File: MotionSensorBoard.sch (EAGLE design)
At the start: 26 parts, among them J1 PRGM, J2 POWER_JACKPTH, U1 ATTINY2313A-SUR, U2 ISO7221ADR, U4 NCP1117ST50T3G, U5 LM1117MPX-3.3

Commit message: updated schematic
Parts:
- removed C5: 0.1uF, SparkFun-Passives:CAP0603-CAP
- removed C8: 10uF, Passives:CAP_POL_AL
- removed JP2: (no value), SparkFun-Connectors:M07
- removed S1: SWITCH, SparkFun-Electromechanical:SWITCH-MOMENTARY-2PTH
- removed Y2: (no value), SparkFun-FreqCtrl:RESONATORPTH
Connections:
- removed net N$1: U1.XTAL2, Y2.1
- removed net N$2: U1.XTAL1, Y2.3
- removed net N$3: JP2.7, U1.PB4
- removed net N$4: JP2.6, U1.PB3
- removed net N$5: JP2.5, U1.PB2
- removed net N$6: JP2.4, U1.PB1
- net 3.3V: no longer JP2.2
- net GND: now also JP1.1; no longer C5.2, C8.-, JP1.3, JP2.1, S1.1, Y2.2
- net RESET: no longer C5.1, S1.2
- net SIGIN: now also JP1.3; no longer JP1.1, JP2.3
- net VIN: no longer C8.+
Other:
- moved on the sheet: C3, C4, R1, U$2, U1, U2

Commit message: Schematic Updated
Schematic Rev A major revisions complete
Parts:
- removed U1: ATTINY2313A-SUR, microcontrollers-atmel:ATTINY2313A-SUR
- added JP4: M02PTH, SparkFun-Connectors:M02PTH
- added Q1, Q2: BSS138, SparkFun-DiscreteSemi:MOSFET-NCHANNELBSS123LT1G
- added R2, R3, R6, R7: 4.7k, SparkFun-Resistors:RESISTOR0603
- added R4: PHOTOCELLPTH, SparkFun-Sensors:PHOTOCELLPTH
- added R5: 10k, SparkFun-Resistors:RESISTOR0603
- added U3: BMP180, SparkFun-Sensors:BMP180
- added U6: HTU21DSMD, SparkFun-Sensors:HTU21DSMD
- added U7: ATMEGA328P, SparkFun-DigitalIC:ATMEGA328_SMT
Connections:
- new net LHT: R4.P$1, R5.2, U7.PC0(ADC0)
- new net SCL_3_3V: Q2.S, R2.1, U3.SCL, U6.SCK
- new net SCL_5V: Q2.D, R6.1, U7.PC5(ADC5/SCL)
- new net SDA_3_3V: Q1.S, R3.1, U3.SDA, U6.DATA
- new net SDA_5V: Q1.D, R7.1, U7.PC4(ADC4/SDA)
- net 3.3V: now also Q1.G, Q2.G, R2.2, R3.2, U3.VDD, U3.VDDIO, U6.VDD
- net 5V: now also R4.P$2, R6.2, R7.2, U7.AVCC, U7.VCC@1, U7.VCC@2; no longer U1.VCC
- net GND: now also JP4.1, R5.1, U3.GND, U6.GND@2, U6.GND@7, U7.AGND, U7.GND@1, U7.GND@2; no longer U1.GND
- net MISO: now also U7.PB4(MISO); no longer U1.PB6
- net MOSI: now also U7.PB3(MOSI/OC2); no longer U1.PB5
- net RESET: now also U7.PC6(/RESET); no longer U1.!RESET
- net RXD: now also U7.PD0(RXD); no longer U1.RXD
- net SCK: now also U7.PB5(SCK); no longer U1.PB7
- net SIGIN: now also U7.PD5(T1); no longer U1.PB0
- net TXD: now also U7.PD1(TXD); no longer U1.TXD
- net VIN: now also JP4.2
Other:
- note added: "A"
- note added: "Ambient Light Sensor"
- note added: "Pressure Sensor"
- note added: "Temperature and Humidity Sensor"
- note removed: "0"
- moved on the sheet: C1, C2, C7, J1, J2, JP1, LED4, R1, R10, U4, U5

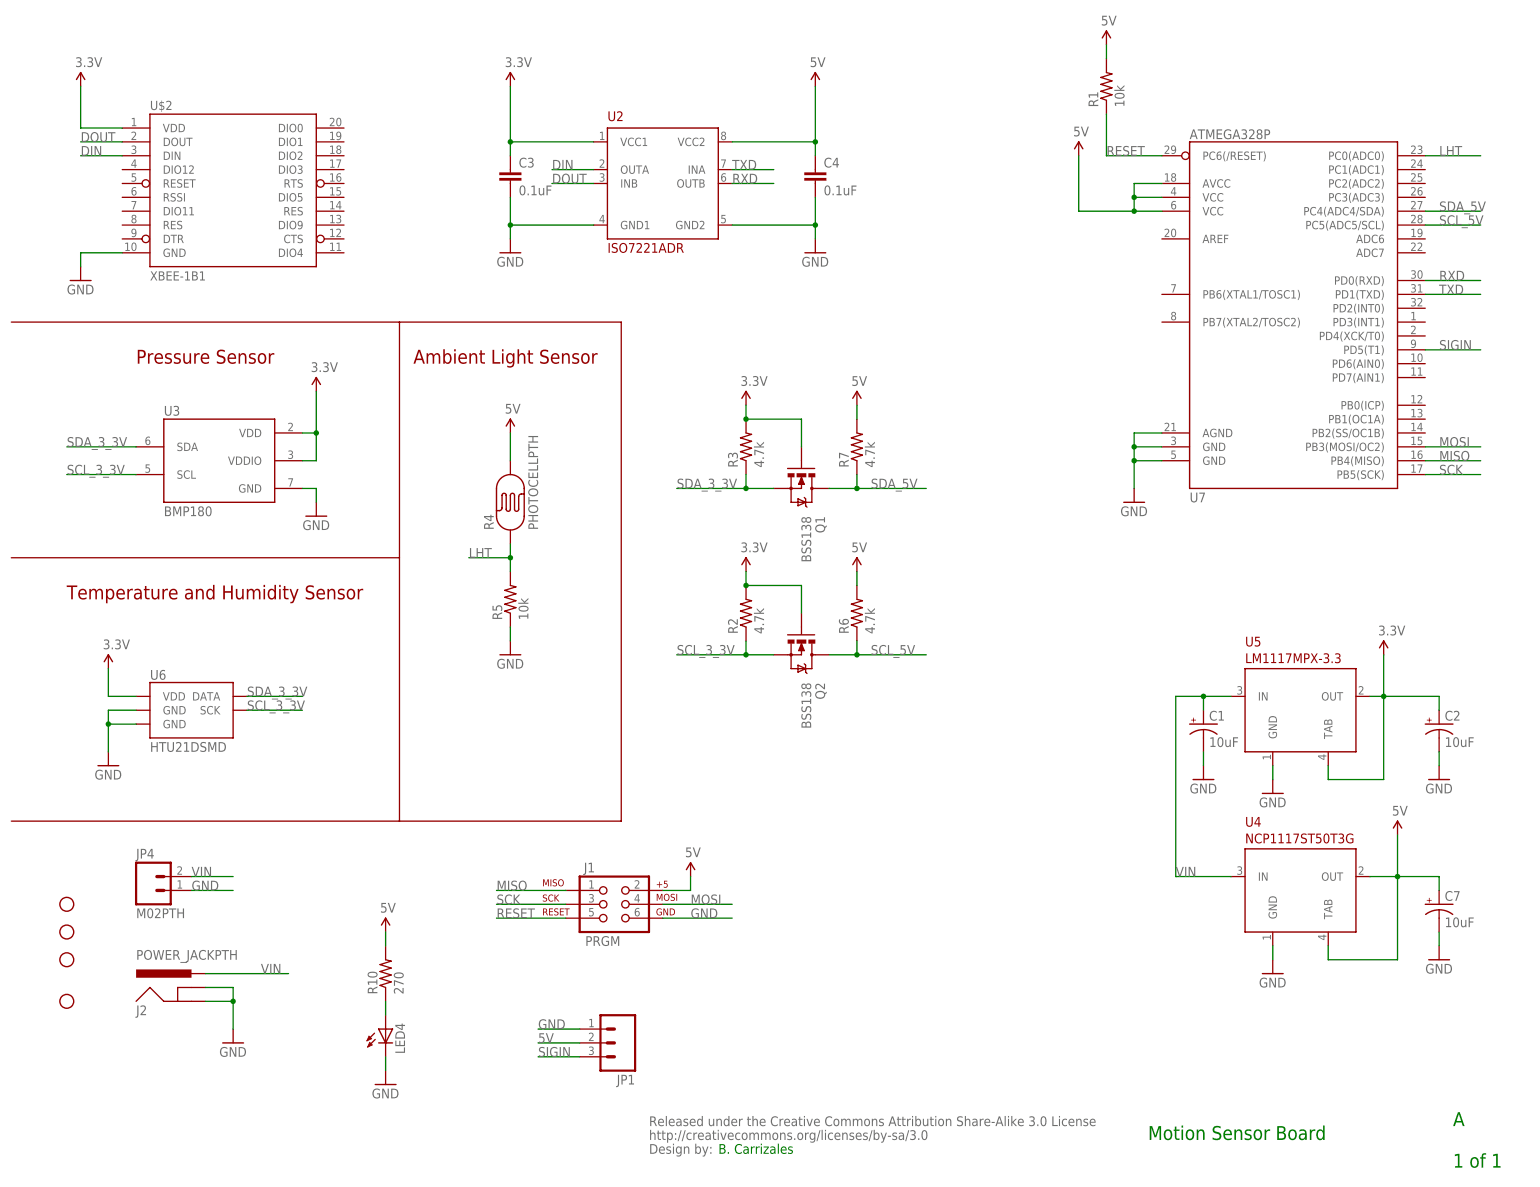
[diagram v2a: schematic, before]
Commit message: updated board layout and generated Gerbers
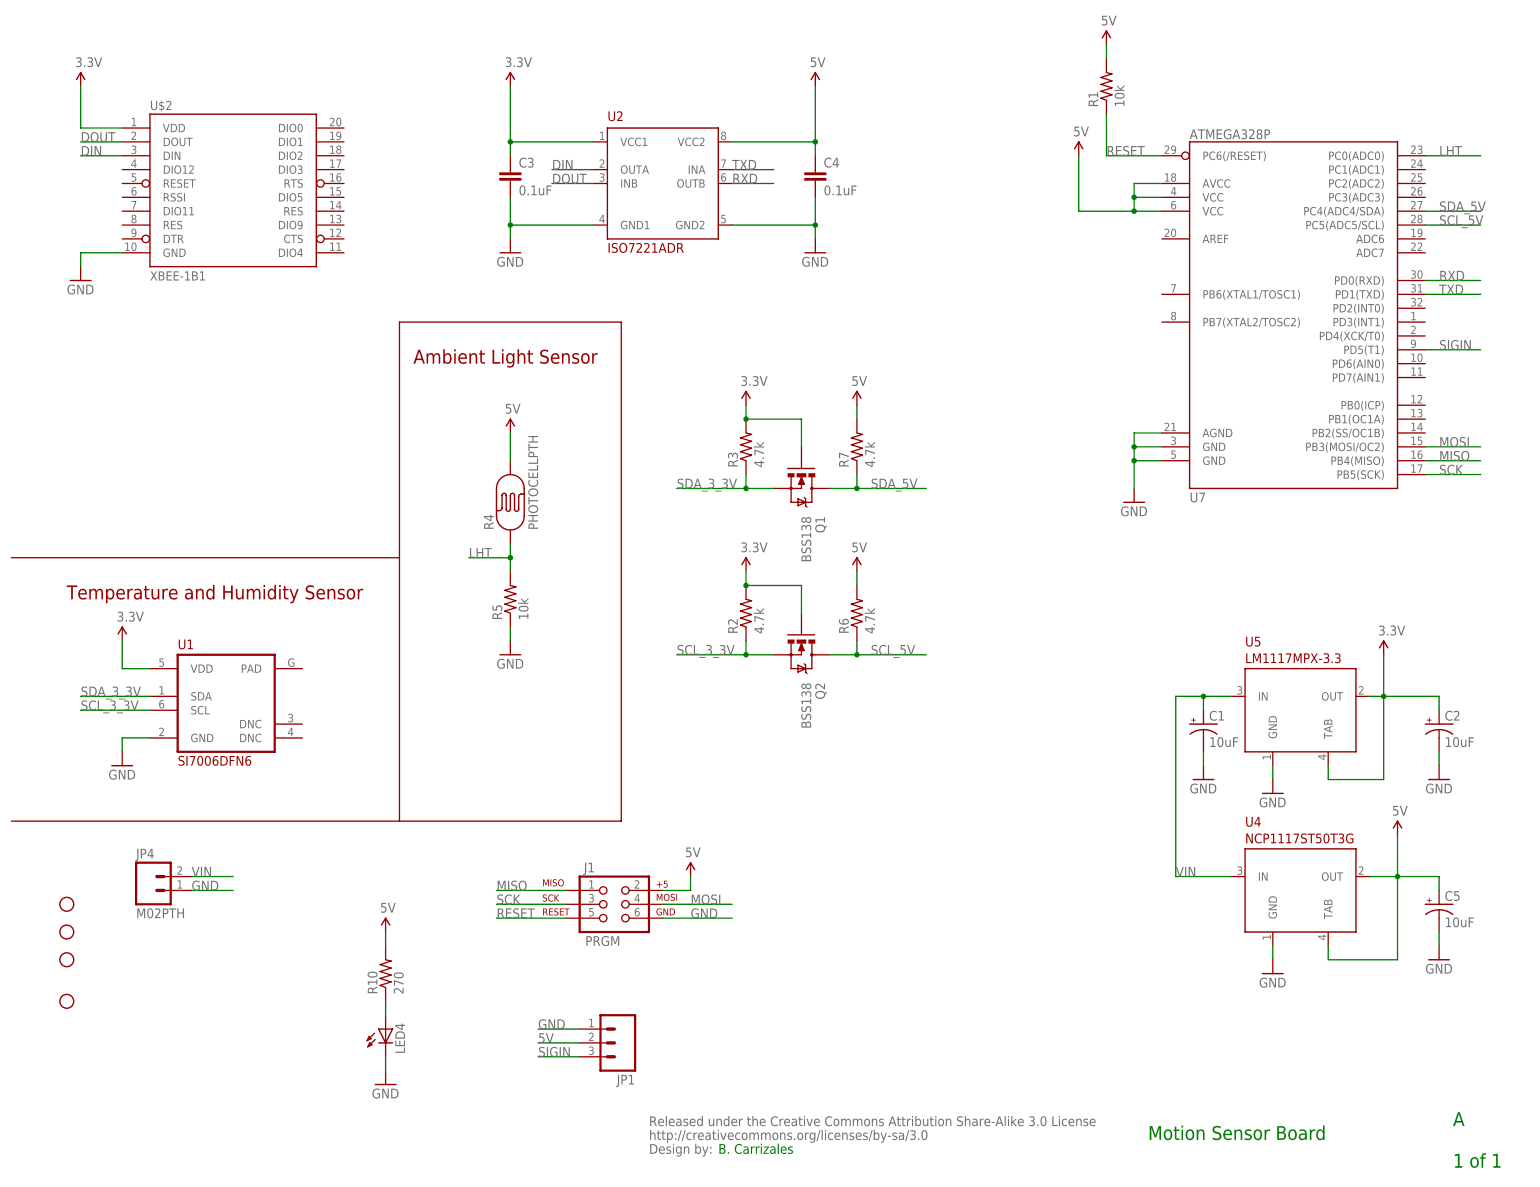
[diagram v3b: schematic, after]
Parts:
- removed C7: 10uF, Passives:CAP_POL_AL
- removed J2: POWER_JACKPTH, SparkFun-Connectors:POWER_JACKPTH
- removed U3: BMP180, SparkFun-Sensors:BMP180
- removed U6: HTU21DSMD, SparkFun-Sensors:HTU21DSMD
- added C5: 10uF, SparkFun-Passives:CAP_POL6032
- added U1: SI7006DFN6, DigitalICs:SI7006DFN6
- C1, C2: device Passives:CAP_POL_AL -> SparkFun-Passives:CAP_POL6032
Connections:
- net 3.3V: now also U1.VDD; no longer U3.VDD, U3.VDDIO, U6.VDD
- net 5V: now also C5.+; no longer C7.+
- net GND: now also C5.-, U1.GND; no longer C7.-, J2.GND, J2.GNDBREAK, U3.GND, U6.GND@2, U6.GND@7
- net SCL_3_3V: now also U1.SCL; no longer U3.SCL, U6.SCK
- net SDA_3_3V: now also U1.SDA; no longer U3.SDA, U6.DATA
- net VIN: no longer J2.PWR
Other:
- note removed: "Pressure Sensor"
